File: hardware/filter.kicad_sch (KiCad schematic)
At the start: 55 parts, among them J11 Pots Main, J12 Pots Front, Q1 KSC1815, Q2 KSC1815, U1 NJM4558D, U2 NJM4558D, U4 NJM4558D, U5 NJM4558D

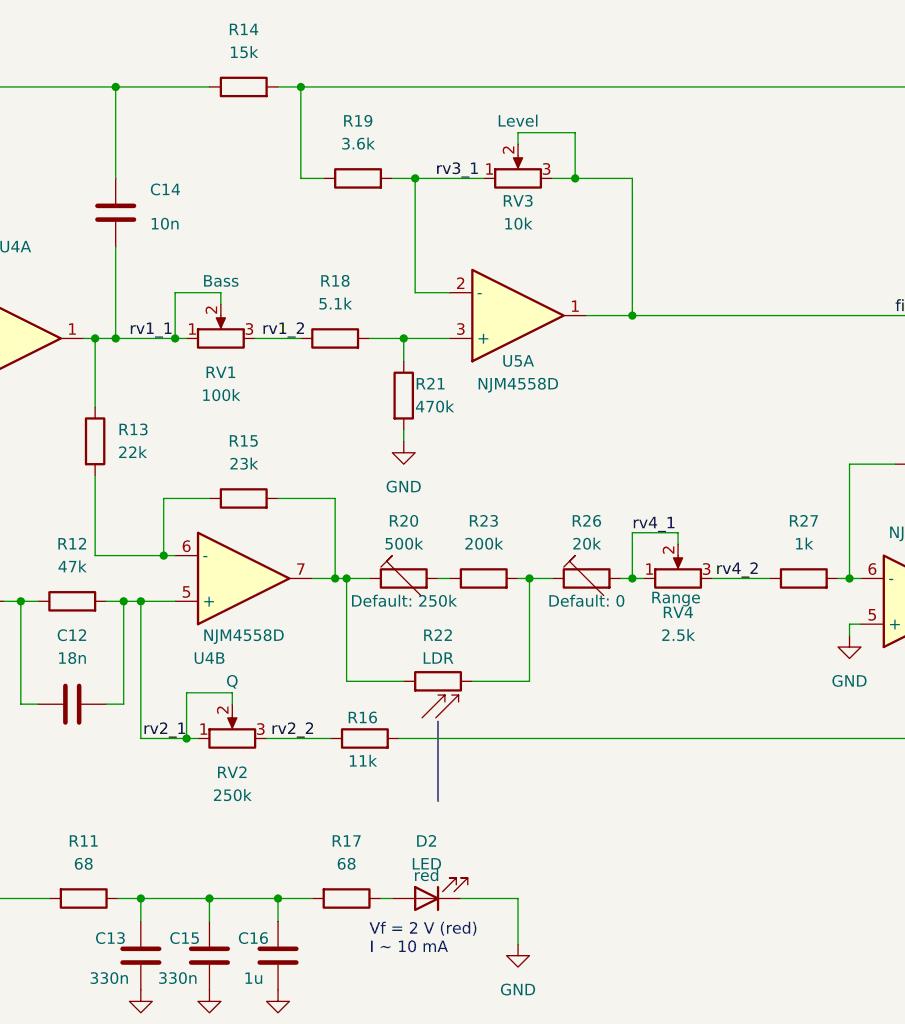
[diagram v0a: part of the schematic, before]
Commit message: Swap pots in schematic (now including mounting pins)
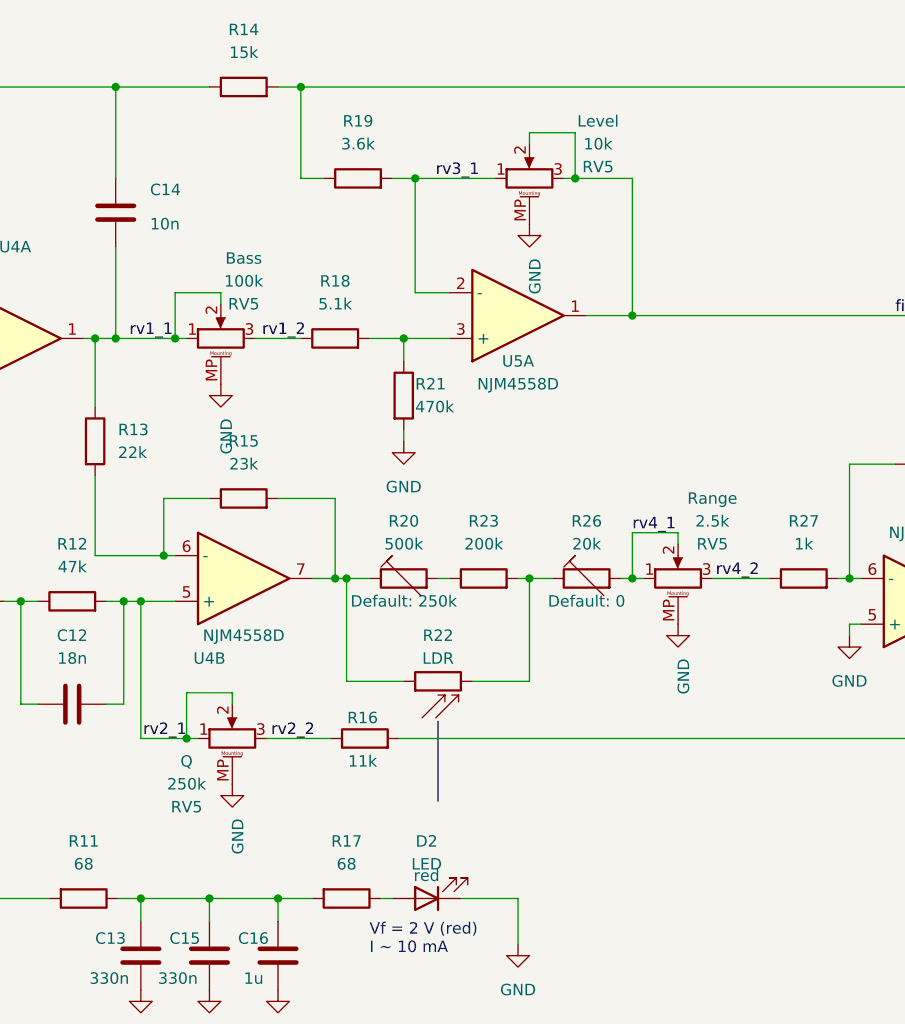
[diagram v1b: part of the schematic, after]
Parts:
- removed RV1: 100k, Potentiometer_THT:Potentiometer_TT_P0915N, symbol Device:R_Potentiometer
- removed RV2: 250k, Potentiometer_THT:Potentiometer_TT_P0915N, symbol Device:R_Potentiometer
- removed RV3: 10k, Potentiometer_THT:Potentiometer_TT_P0915N, symbol Device:R_Potentiometer
- removed RV4: 2.5k, Potentiometer_THT:Potentiometer_TT_P0915N, symbol Device:R_Potentiometer
- added RV5: 100k, uMidi-wah:Bourns PC Axial Rear Mounting Bracket, symbol Device:R_Potentiometer_MountingPin
- added RV5: 10k, uMidi-wah:Bourns PC Axial Rear Mounting Bracket, symbol Device:R_Potentiometer_MountingPin
- added RV5: 2.5k, uMidi-wah:Bourns PC Axial Rear Mounting Bracket, symbol Device:R_Potentiometer_MountingPin
- added RV5: 250k, uMidi-wah:Bourns PC Axial Rear Mounting Bracket, symbol Device:R_Potentiometer_MountingPin
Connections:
- net GND: now also RV5.MP (MountPin), RV5.MP (MountPin), RV5.MP (MountPin), RV5.MP (MountPin)
- net filter_out: now also RV5.2, RV5.3
- net rv1_1: now also RV5.1, RV5.2
- net rv1_2: now also RV5.3
- net rv2_1: now also RV5.1, RV5.2
- net rv2_2: now also RV5.3
- net rv3_1: now also RV5.1
- net rv4_1: now also RV5.1, RV5.2
- net rv4_2: now also RV5.3

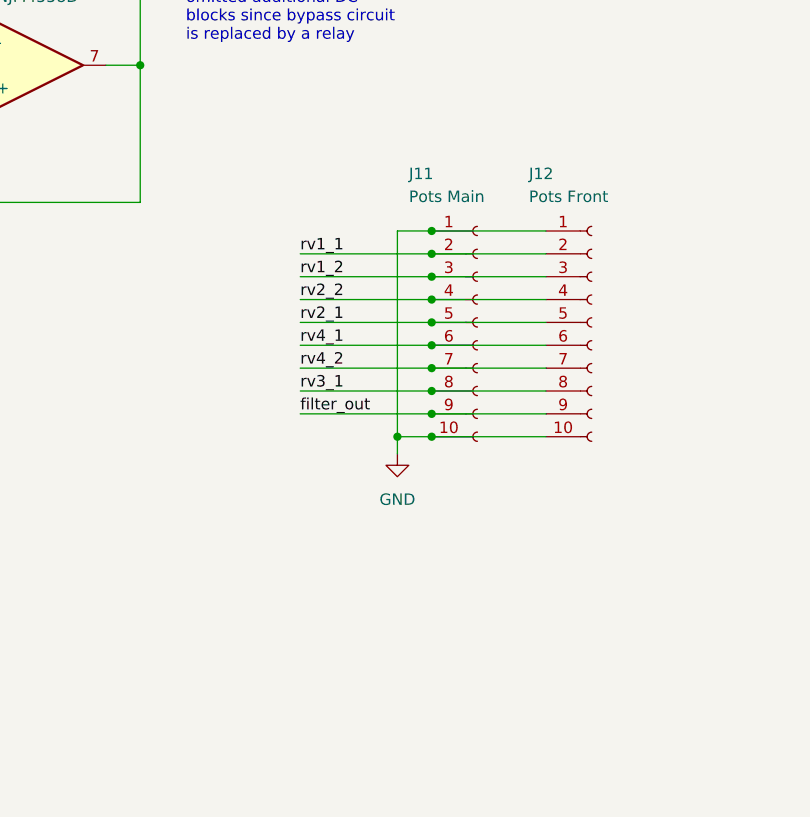
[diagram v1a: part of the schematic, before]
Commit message: Route pretty much everything
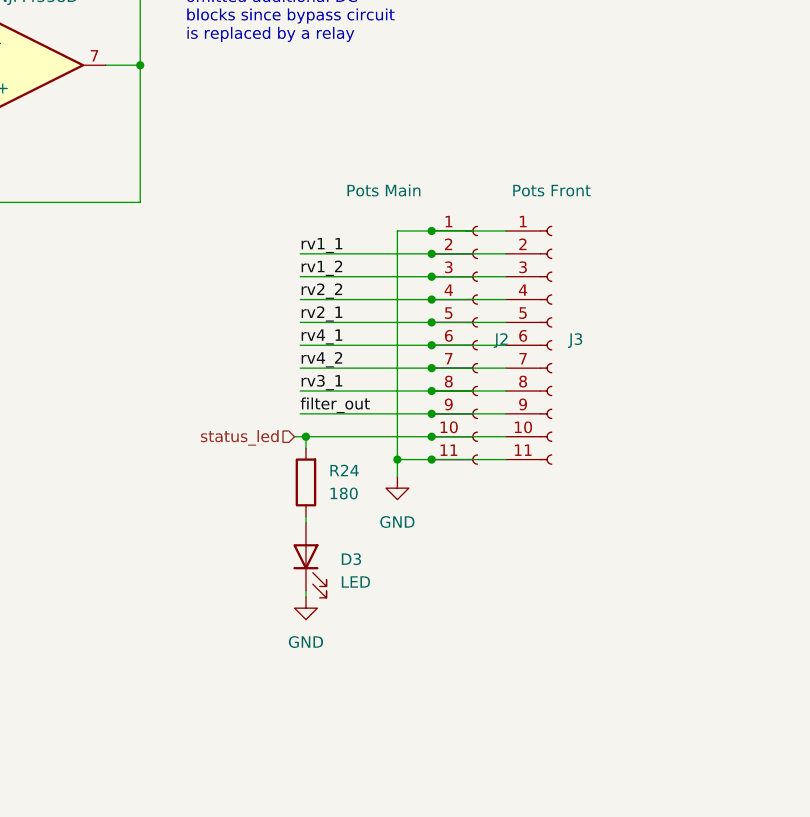
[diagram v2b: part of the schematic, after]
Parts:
- removed J11: Pots Main, Connector_PinHeader_2.54mm:PinHeader_1x10_P2.54mm_Vertical, symbol Connector:Conn_01x10_Socket
- removed J12: Pots Front, Connector_PinHeader_2.54mm:PinHeader_1x10_P2.54mm_Vertical, symbol Connector:Conn_01x10_Socket
- added D3: LED, LED_THT:LED_D5.0mm, symbol Device:LED
- added J2: Pots Main, Connector_PinHeader_2.54mm:PinHeader_1x11_P2.54mm_Vertical, symbol Connector:Conn_01x11_Socket
- added J3: Pots Front, Connector_PinHeader_2.54mm:PinHeader_1x11_P2.54mm_Vertical, symbol Connector:Conn_01x11_Socket
- added R24: 180, Resistor_SMD:R_0805_2012Metric_Pad1.20x1.40mm_HandSolder, symbol Device:R
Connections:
- net GND: now also D3.1 (K), J2.1 (Pin_1), J2.11 (Pin_11), J3.1 (Pin_1), J3.11 (Pin_11)
- net filter_out: now also J2.9 (Pin_9), J3.9 (Pin_9)
- net rv1_1: now also J2.2 (Pin_2), J3.2 (Pin_2)
- net rv1_2: now also J2.3 (Pin_3), J3.3 (Pin_3)
- net rv2_1: now also J2.5 (Pin_5), J3.5 (Pin_5)
- net rv2_2: now also J2.4 (Pin_4), J3.4 (Pin_4)
- net rv3_1: now also J2.8 (Pin_8), J3.8 (Pin_8)
- net rv4_1: now also J2.6 (Pin_6), J3.6 (Pin_6)
- net rv4_2: now also J2.7 (Pin_7), J3.7 (Pin_7)
- new net: D3.2 (A), R24.1
- new net status_led: J2.10 (Pin_10), J3.10 (Pin_10), R24.2

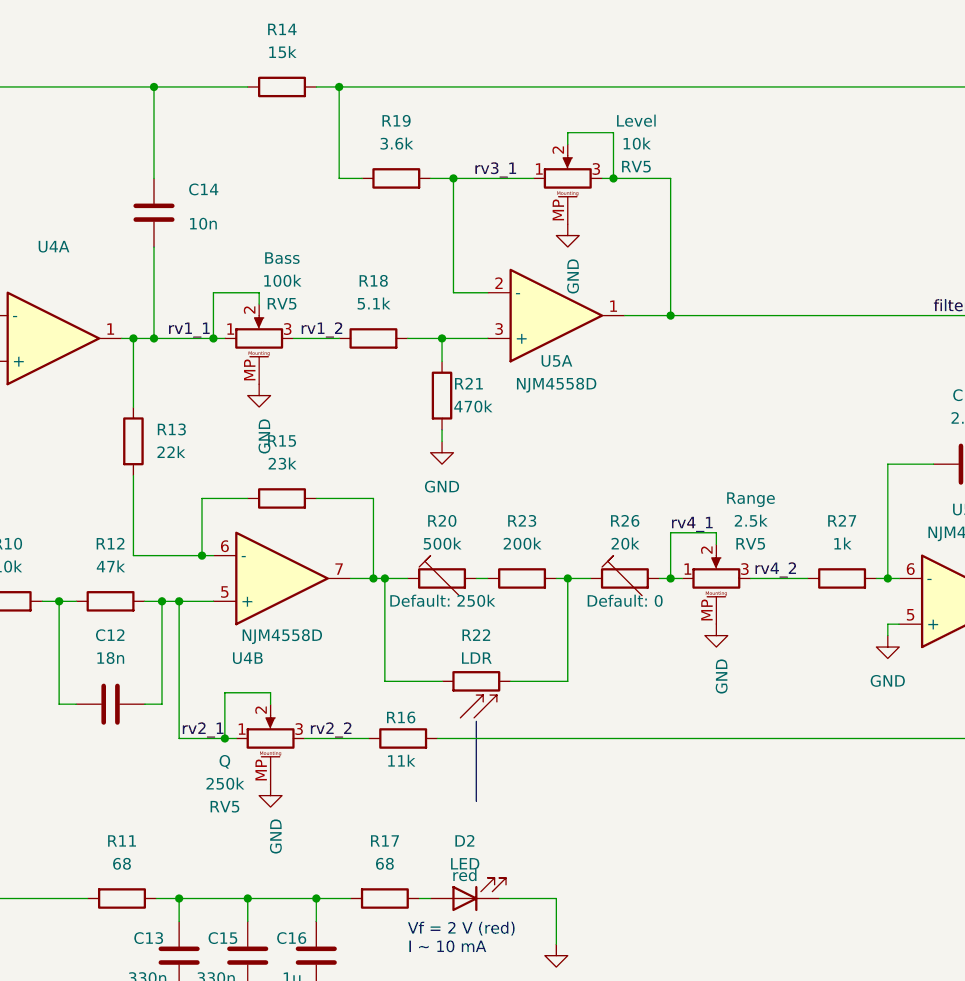
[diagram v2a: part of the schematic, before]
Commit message: Fix range poti value; Fix poti directions; Specify taper types
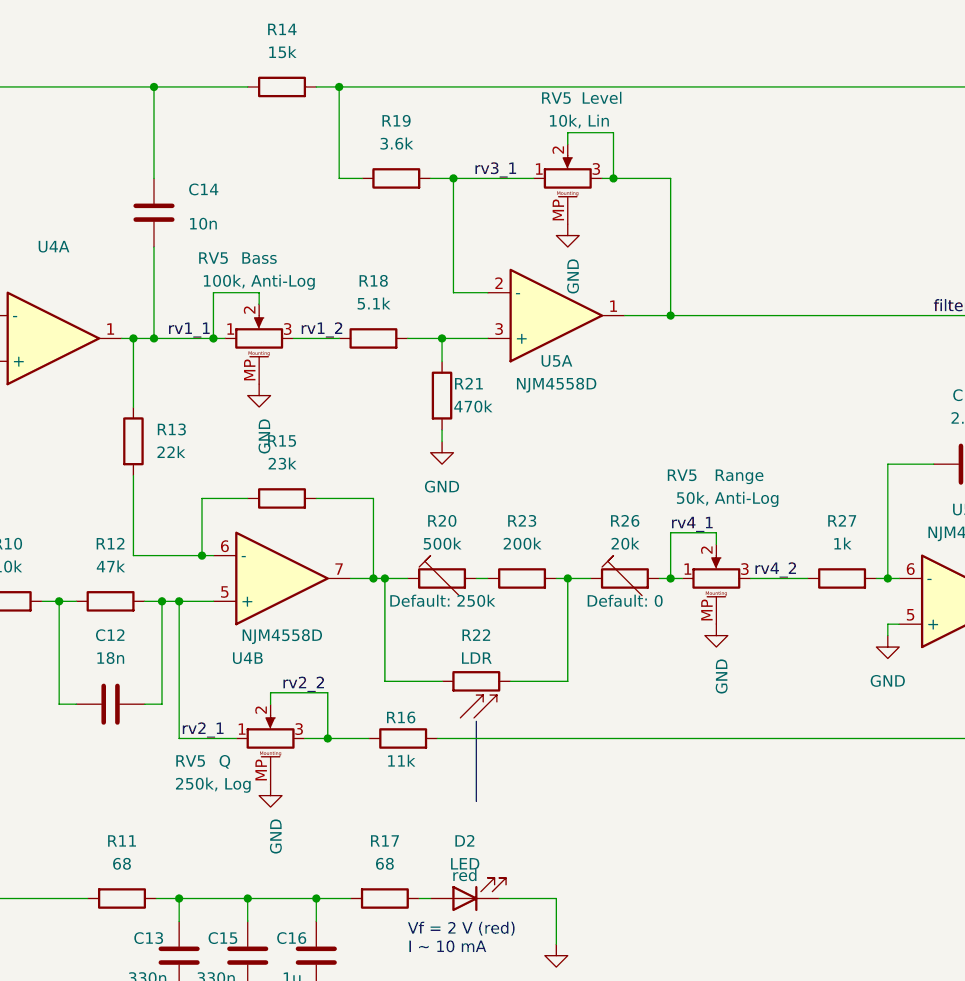
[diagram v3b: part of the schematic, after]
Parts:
- RV5: value 100k -> 100k, Anti-Log
- RV5: value 10k -> 10k, Lin
- RV5: value 2.5k -> 50k, Anti-Log
- RV5: value 250k -> 250k, Log
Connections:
- net rv2_1: no longer RV5.2
- net rv2_2: now also RV5.2
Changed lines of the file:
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@@
   (junction (at 114.3 90.17) (diameter 0) (color 0 0 0 0)
   )
+  (junction (at 128.27 110.49) (diameter 0) (color 0 0 0 0)
+  )
   (junction (at 243.205 123.825) (diameter 0) (color 0 0 0 0)
   )
@@
   (junction (at 127 128.27) (diameter 0) (color 0 0 0 0)
   )
-  (junction (at 116.84 110.49) (diameter 0) (color 0 0 0 0)
-  )
   (junction (at 46.355 110.49) (diameter 0) (color 0 0 0 0)
   )
@@
     (stroke (width 0) (type default))
   )
-  (wire (pts (xy 111.76 110.49) (xy 116.84 110.49))
-    (stroke (width 0) (type default))
-  )
   (wire (pts (xy 140.97 66.04) (xy 140.97 68.58))
     (stroke (width 0) (type default))
@@
     (stroke (width 0) (type default))
   )
-  (wire (pts (xy 116.84 110.49) (xy 116.84 105.41))
-    (stroke (width 0) (type default))
-  )
   (wire (pts (xy 251.46 118.745) (xy 243.205 118.745))
     (stroke (width 0) (type default))
@@
     (stroke (width 0) (type default))
   )
-  (wire (pts (xy 116.84 105.41) (xy 121.92 105.41))
-    (stroke (width 0) (type default))
-  )
   (wire (pts (xy 212.09 63.5) (xy 213.36 63.5))
     (stroke (width 0) (type default))
@@
     (stroke (width 0) (type default))
   )
+  (wire (pts (xy 121.92 105.41) (xy 128.27 105.41))
+    (stroke (width 0) (type default))
+  )
   (wire (pts (xy 161.29 63.5) (xy 166.37 63.5))
     (stroke (width 0) (type default))
@@
     (stroke (width 0) (type default))
   )
-  (wire (pts (xy 116.84 110.49) (xy 118.11 110.49))
+  (wire (pts (xy 111.76 110.49) (xy 118.11 110.49))
     (stroke (width 0) (type default))
   )
@@
     (stroke (width 0) (type default))
   )
-  (wire (pts (xy 125.73 110.49) (xy 132.842 110.49))
+  (wire (pts (xy 125.73 110.49) (xy 128.27 110.49))
     (stroke (width 0) (type default))
   )
@@
     (stroke (width 0) (type default))
   )
+  (wire (pts (xy 128.27 110.49) (xy 132.842 110.49))
+    (stroke (width 0) (type default))
+  )
   (wire (pts (xy 109.22 128.27) (xy 111.76 128.27))
     (stroke (width 0) (type default))
@@
   )
   (wire (pts (xy 78.74 104.14) (xy 78.74 107.95))
+    (stroke (width 0) (type default))
+  )
+  (wire (pts (xy 128.27 105.41) (xy 128.27 110.49))
     (stroke (width 0) (type default))
   )
@@
     (effects (font (size 1.27 1.27)) (justify left bottom))
   )
-  (label "rv2_2" (at 126.238 110.49 0) (fields_autoplaced)
+  (label "rv2_2" (at 123.19 105.41 0) (fields_autoplaced)
     (effects (font (size 1.27 1.27)) (justify left bottom))
   )
@@
   (symbol (lib_id "Device:R_Potentiometer_MountingPin") (at 120.65 66.04 90) (unit 1)
     (in_bom yes) (on_board yes) (dnp no)
-    (property "Reference" "RV5" (at 123.19 62.23 90)
-      (effects (font (size 1.27 1.27)))
-    )
-    (property "Value" "100k" (at 123.19 59.69 90)
+    (property "Reference" "RV5" (at 115.57 57.15 90)
+      (effects (font (size 1.27 1.27)))
+    )
+    (property "Value" "100k, Anti-Log" (at 120.65 59.69 90)
       (effects (font (size 1.27 1.27)))
     )
@@
       (effects (font (size 1.27 1.27)) hide)
     )
-    (property "Datasheet" "https://www.tme.eu/Document/24f604905978b51bc66e017b5b3c4a2b/PCW1J-B24-KAB502L.pdf" (at 120.65 66.04 0)
-      (effects (font (size 1.27 1.27)) hide)
-    )
-    (property "Function" "Bass" (at 123.19 57.15 90)
+    (property "Datasheet" "" (at 120.65 66.04 0)
+      (effects (font (size 1.27 1.27)) hide)
+    )
+    (property "Function" "Bass" (at 120.65 57.15 90)
       (effects (font (size 1.27 1.27)))
     )
@@
   (symbol (lib_id "Device:R_Potentiometer_MountingPin") (at 154.94 48.26 90) (unit 1)
     (in_bom yes) (on_board yes) (dnp no)
-    (property "Reference" "RV5" (at 162.56 46.99 90)
-      (effects (font (size 1.27 1.27)))
-    )
-    (property "Value" "10k" (at 162.56 44.45 90)
+    (property "Reference" "RV5" (at 153.67 39.37 90)
+      (effects (font (size 1.27 1.27)))
+    )
+    (property "Value" "10k, Lin" (at 156.21 41.91 90)
       (effects (font (size 1.27 1.27)))
     )
@@
       (effects (font (size 1.27 1.27)) hide)
     )
-    (property "Datasheet" "https://www.tme.eu/Document/24f604905978b51bc66e017b5b3c4a2b/PCW1J-B24-KAB502L.pdf" (at 154.94 48.26 0)
-      (effects (font (size 1.27 1.27)) hide)
-    )
-    (property "Function" "Level" (at 162.56 41.91 90)
+    (property "Datasheet" "" (at 154.94 48.26 0)
+      (effects (font (size 1.27 1.27)) hide)
+    )
+    (property "Function" "Level" (at 158.75 39.37 90)
       (effects (font (size 1.27 1.27)))
     )
@@
   (symbol (lib_id "Device:R_Potentiometer_MountingPin") (at 171.45 92.71 90) (unit 1)
     (in_bom yes) (on_board yes) (dnp no)
-    (property "Reference" "RV5" (at 175.26 88.9 90)
-      (effects (font (size 1.27 1.27)))
-    )
-    (property "Value" "2.5k" (at 175.26 86.36 90)
+    (property "Reference" "RV5" (at 167.64 81.28 90)
+      (effects (font (size 1.27 1.27)))
+    )
+    (property "Value" "50k, Anti-Log" (at 172.72 83.82 90)
       (effects (font (size 1.27 1.27)))
     )
@@
       (effects (font (size 1.27 1.27)) hide)
     )
-    (property "Datasheet" "https://www.tme.eu/Document/24f604905978b51bc66e017b5b3c4a2b/PCW1J-B24-KAB502L.pdf" (at 171.45 92.71 0)
-      (effects (font (size 1.27 1.27)) hide)
-    )
-    (property "Function" "Range" (at 175.26 83.82 90)
+    (property "Datasheet" "" (at 171.45 92.71 0)
+      (effects (font (size 1.27 1.27)) hide)
+    )
+    (property "Function" "Range" (at 173.99 81.28 90)
       (effects (font (size 1.27 1.27)))
     )
@@
   (symbol (lib_id "Device:R_Potentiometer_MountingPin") (at 121.92 110.49 90) (unit 1)
     (in_bom yes) (on_board yes) (dnp no)
-    (property "Reference" "RV5" (at 116.84 118.11 90)
-      (effects (font (size 1.27 1.27)))
-    )
-    (property "Value" "250k" (at 116.84 115.57 90)
+    (property "Reference" "RV5" (at 113.03 113.03 90)
+      (effects (font (size 1.27 1.27)))
+    )
+    (property "Value" "250k, Log" (at 115.57 115.57 90)
       (effects (font (size 1.27 1.27)))
     )
@@
       (effects (font (size 1.27 1.27)) hide)
     )
-    (property "Datasheet" "https://www.tme.eu/Document/24f604905978b51bc66e017b5b3c4a2b/PCW1J-B24-KAB502L.pdf" (at 121.92 110.49 0)
-      (effects (font (size 1.27 1.27)) hide)
-    )
+    (property "Datasheet" "" (at 121.92 110.49 0)
+      (effects (font (size 1.27 1.27)) hide)
+    )
